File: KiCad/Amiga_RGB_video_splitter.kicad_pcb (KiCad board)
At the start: 4 copper layers, 57.5 x 60 mm, 35 parts, among them J1 DB23_Female-Connector, J2 DB15_Female_HighDensity_Mount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, J3 KMDGX-9S-BS-1, J4 PJ-320A, J5 MSS22D18 3Pin Slide Toggle Sw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, J6 MSS22D18 3Pin Slide Toggle Sw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, J7 Conn_01x01, U1 THS7374IPWR, U2 74HCT2G17, U3 74HCT2G14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

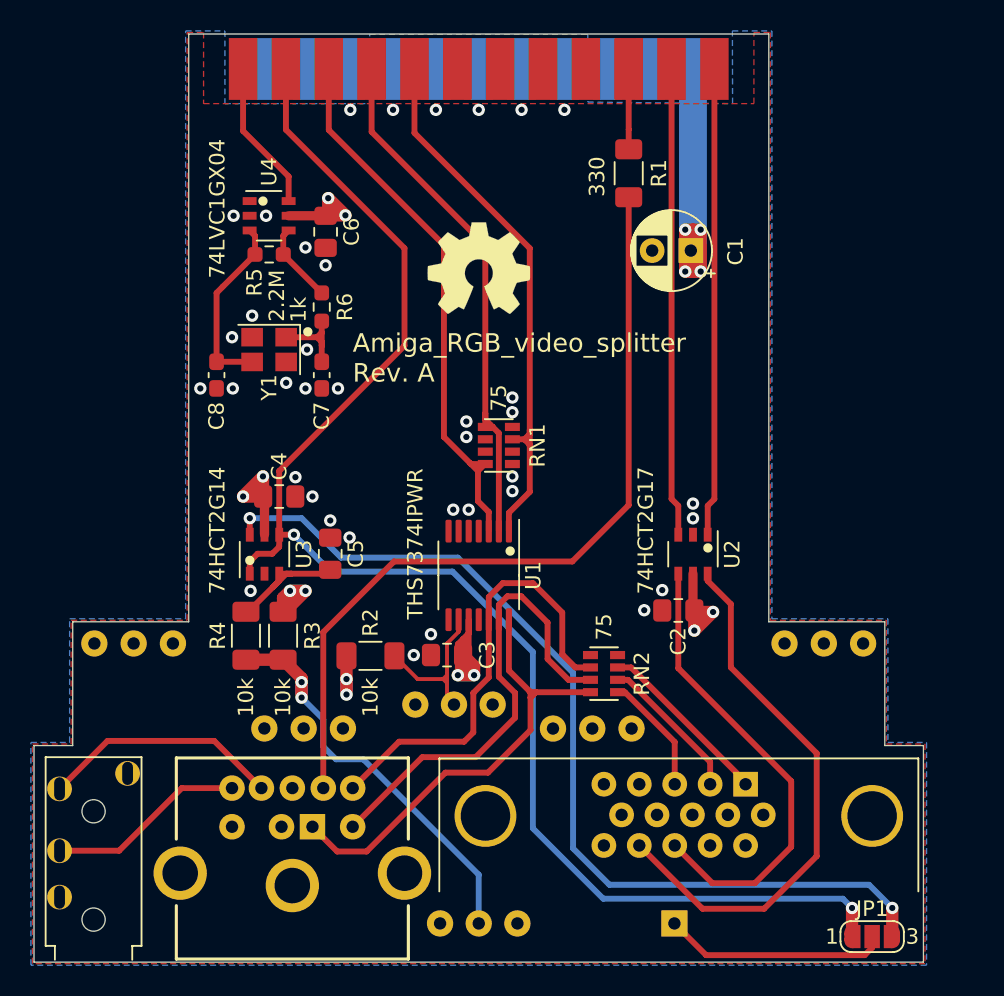
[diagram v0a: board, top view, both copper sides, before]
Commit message: Fix placement of support pinheaders and RN2, some rerouting and silkscreen fixes, bump revision to Rev B
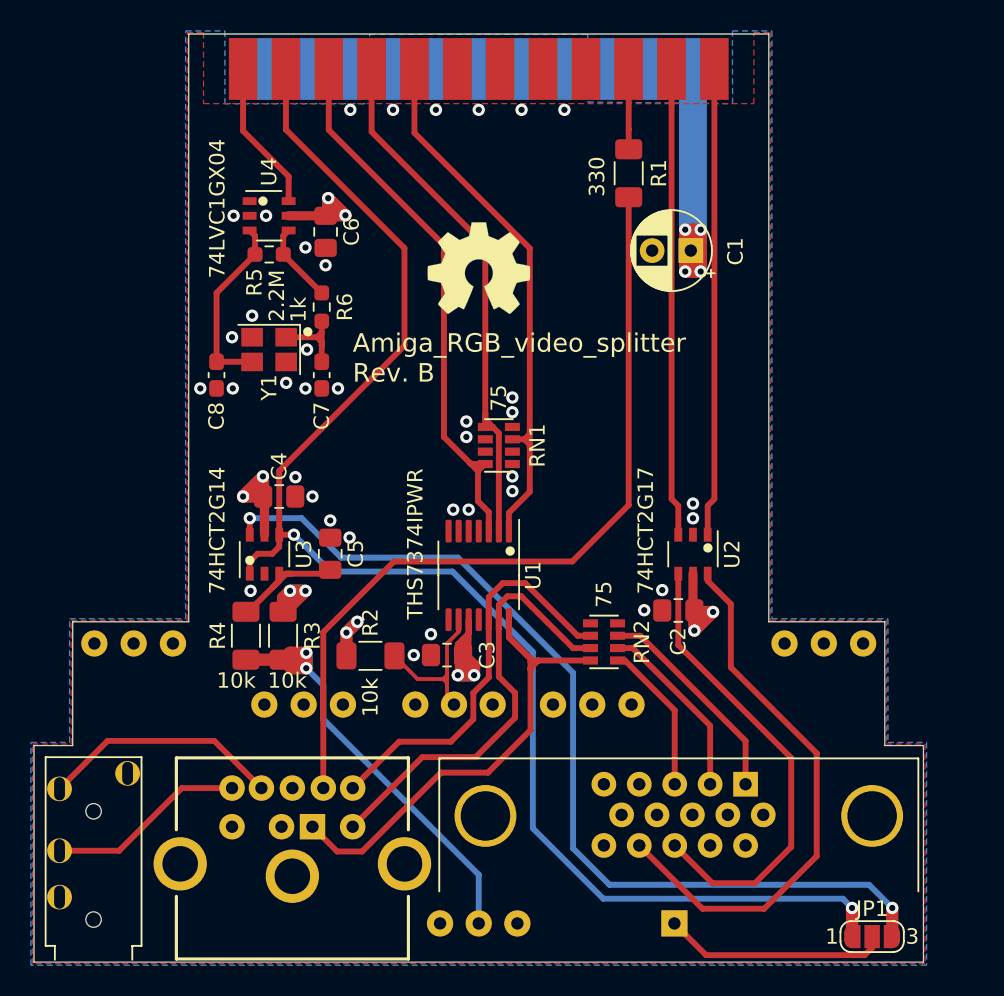
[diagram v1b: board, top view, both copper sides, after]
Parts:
- moved RN2 2.05 mm to (155.8, 124.3)
- moved REF** 1.55 mm to (152.5, 128.3)
- moved REF** 1.54 mm to (133.8, 128.3)
- moved J3 0.60 mm to (137.0, 135.6)
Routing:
- net Net-(J6-Pad2): track 26.7 -> 32.3 mm
- net RED: track 29.2 -> 26.3 mm
- net VGA_R: track 11.5 -> 13.9 mm
- net GREEN: track 30.9 -> 28.7 mm
- net VGA_G: track 9.62 -> 11.9 mm
- net BLUE: track 30.5 -> 32.6 mm
- net VGA_B: track 7.76 -> 9.81 mm
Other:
- board text added: "Amiga_RGB_video_splitter Rev. B"
- board text removed: "Amiga_RGB_video_splitter Rev. A"

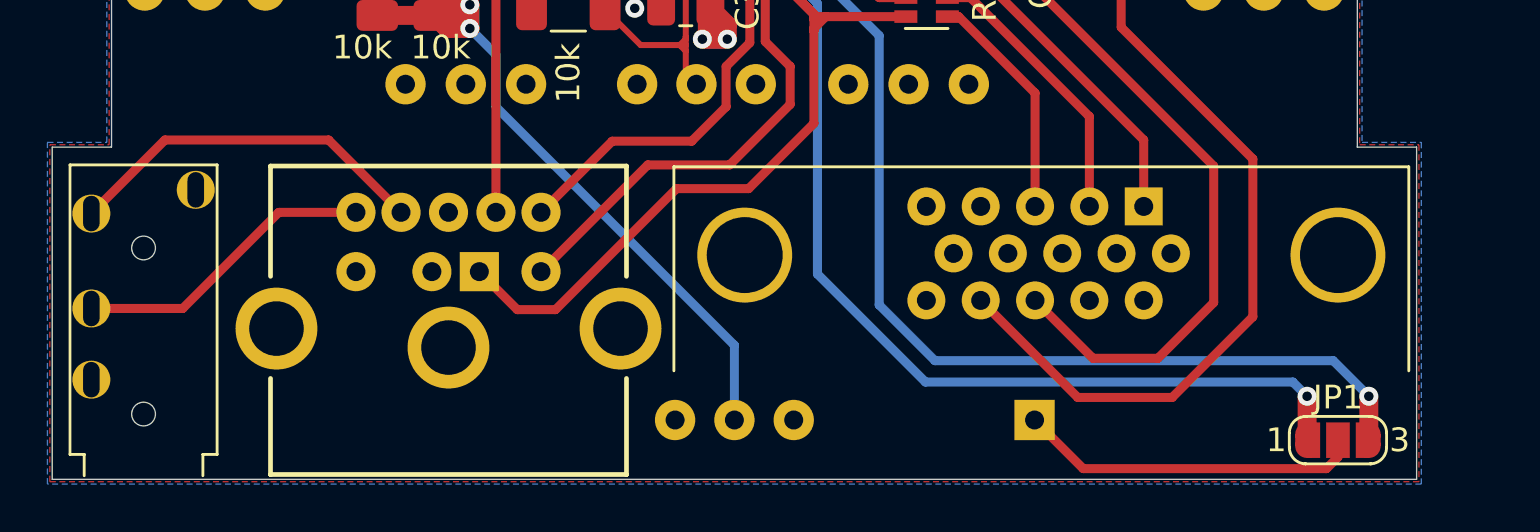
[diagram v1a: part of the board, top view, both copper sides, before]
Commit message: Relocate the PAL/NTSC 3Pin Slide Toggle Switch
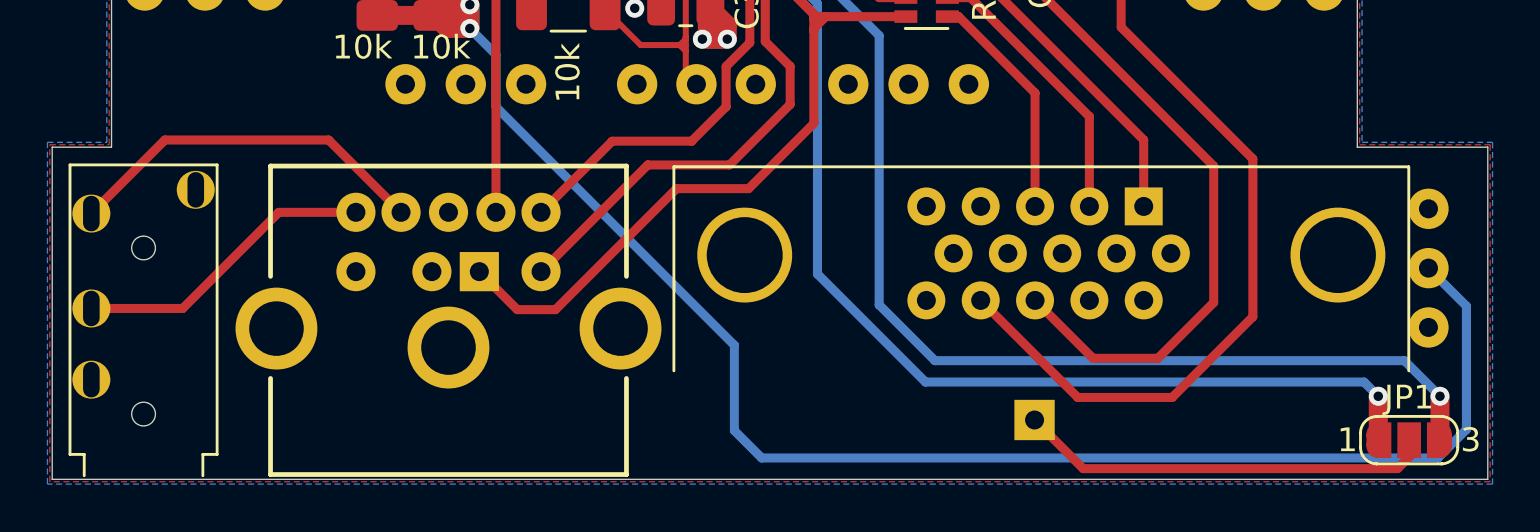
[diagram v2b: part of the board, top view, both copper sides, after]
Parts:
- moved J6 29.9 mm to (176.9, 136.1), turned to 180 degrees
- moved JP1 3.00 mm to (176.1, 143.3)
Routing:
- net Net-(J6-Pad2): track 32.3 -> 72.1 mm
- net OE: track 61.5 -> 64.5 mm
- net XCLKEN: track 96.1 -> 99.1 mm
- net Net-(J7-Pad1): track 14.6 -> 17.6 mm
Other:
- board size 57.5 x 60 mm -> 60.5 x 60 mm

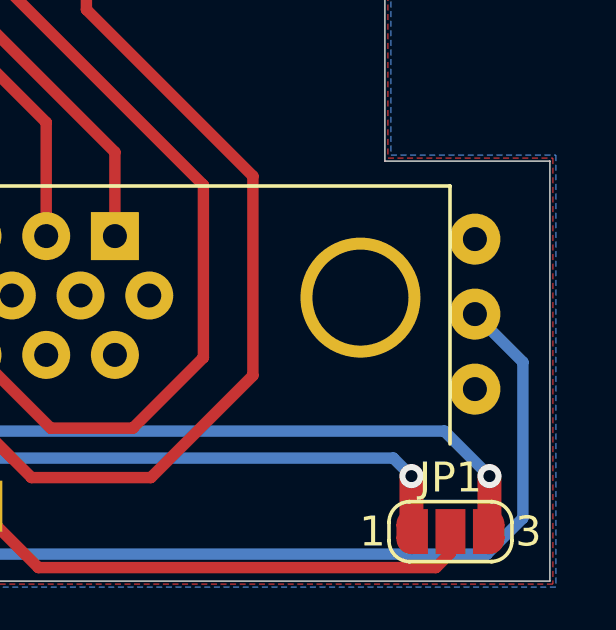
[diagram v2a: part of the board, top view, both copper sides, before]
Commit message: Silkscreen fix on VGA connector footprint
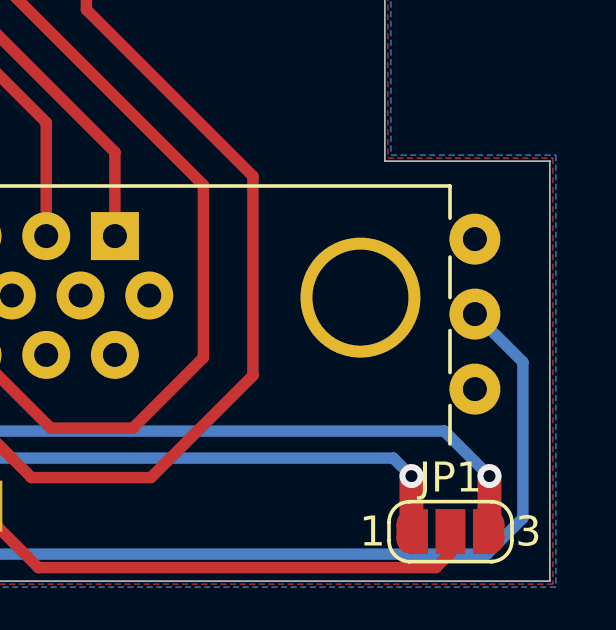
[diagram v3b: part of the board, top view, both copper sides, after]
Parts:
- J6: moved to F.Cu

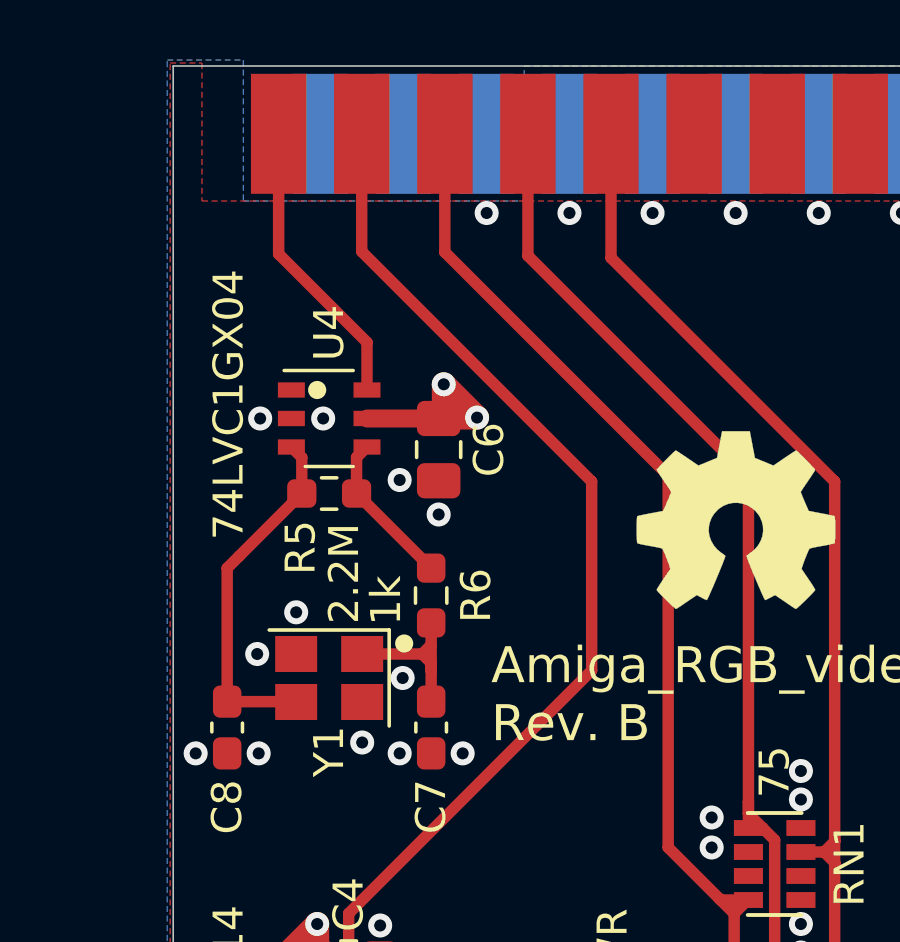
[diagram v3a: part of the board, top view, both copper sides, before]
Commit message: Add damping 150 Ohm series resistor on XCLK out, bump to Rev. C
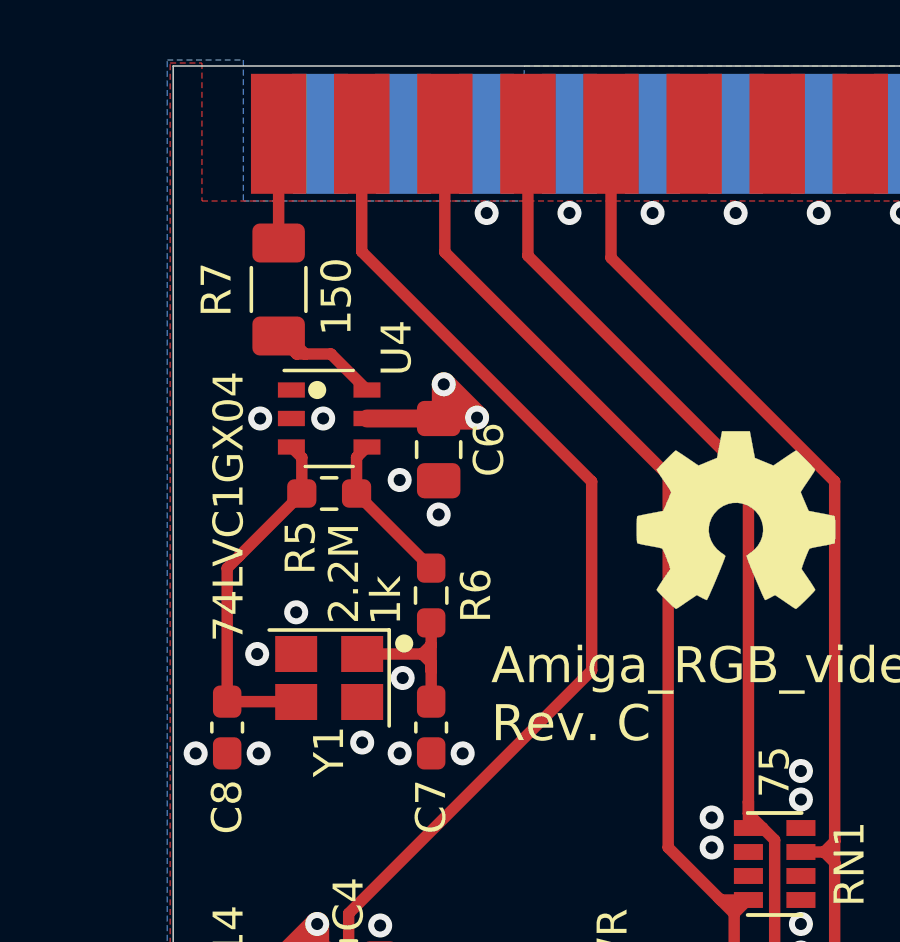
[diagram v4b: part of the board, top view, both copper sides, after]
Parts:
- added R7: 150, Resistor_SMD:R_1206_3216Metric_Pad1.30x1.75mm_HandSolder, F.Cu at (132.5, 92.5)
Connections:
- U4 pad 6: XCLK -> Net-(R7-Pad1)
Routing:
- net XCLK: track 9.76 -> 3.64 mm
- net Net-(R7-Pad1): track 0.00 -> 4.82 mm
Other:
- board text added: "150"
- board text added: "Amiga_RGB_video_splitter Rev. C"
- board text removed: "Amiga_RGB_video_splitter Rev. B"
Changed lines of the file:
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@@
   (general
     (thickness 1.6)
-    (drawings 31)
-    (tracks 345)
+    (drawings 32)
+    (tracks 349)
     (zones 0)
-    (modules 35)
-    (nets 57)
+    (modules 36)
+    (nets 58)
   )
   (page A4)
@@
   (net 55 "Net-(C8-Pad1)")
   (net 56 "Net-(J7-Pad1)")
+  (net 57 "Net-(R7-Pad1)")
   (net_class Default "This is the default net class."
     (clearance 0.1524)
@@
     (add_net "Net-(J7-Pad1)")
     (add_net "Net-(R5-Pad2)")
+    (add_net "Net-(R7-Pad1)")
     (add_net "Net-(RN1-Pad3)")
     (add_net "Net-(RN1-Pad6)")
@@
     (add_net XCLK)
     (add_net XCLKEN)
+  )
+  (module Resistor_SMD:R_1206_3216Metric_Pad1.30x1.75mm_HandSolder (layer F.Cu)
+    (at 132.465 92.45 90)
+    (descr "Resistor SMD 1206 (3216 Metric), square (rectangular) end terminal, IPC_7351 nominal with elongated pad for handsoldering. (Body size source: IPC-SM-782 page 72, https://www.pcb-3d.com/wordpress/wp-content/uploads/ipc-sm-782a_amendment_1_and_2.pdf), generated with kicad-footprint-generator")
+    (tags "resistor handsolder")
+    (attr smd)
+    (fp_text reference R7 (at 0 -2.065 90) (layer F.SilkS)
+      (effects (font (size 1 1) (thickness 0.15)))
+    )
+    (fp_text value 150 (at 0 1.82 90) (layer F.Fab) hide
+      (effects (font (size 1 1) (thickness 0.15)))
+    )
+    (fp_line (start 2.45 1.12) (end -2.45 1.12) (layer F.CrtYd) (width 0.05))
+    (fp_line (start 2.45 -1.12) (end 2.45 1.12) (layer F.CrtYd) (width 0.05))
+    (fp_line (start -2.45 -1.12) (end 2.45 -1.12) (layer F.CrtYd) (width 0.05))
+    (fp_line (start -2.45 1.12) (end -2.45 -1.12) (layer F.CrtYd) (width 0.05))
+    (fp_line (start -0.727064 0.91) (end 0.727064 0.91) (layer F.SilkS) (width 0.12))
+    (fp_line (start -0.727064 -0.91) (end 0.727064 -0.91) (layer F.SilkS) (width 0.12))
+    (fp_line (start 1.6 0.8) (end -1.6 0.8) (layer F.Fab) (width 0.1))
+    (fp_line (start 1.6 -0.8) (end 1.6 0.8) (layer F.Fab) (width 0.1))
+    (fp_line (start -1.6 -0.8) (end 1.6 -0.8) (layer F.Fab) (width 0.1))
+    (fp_line (start -1.6 0.8) (end -1.6 -0.8) (layer F.Fab) (width 0.1))
+    (fp_text user %R (at 0 0 90) (layer F.Fab) hide
+      (effects (font (size 0.8 0.8) (thickness 0.12)))
+    )
+    (pad 2 smd roundrect (at 1.55 0 90) (size 1.3 1.75) (layers F.Cu F.Paste F.Mask) (roundrect_rratio 0.192308)
+      (net 18 XCLK))
+    (pad 1 smd roundrect (at -1.55 0 90) (size 1.3 1.75) (layers F.Cu F.Paste F.Mask) (roundrect_rratio 0.192308)
+      (net 57 "Net-(R7-Pad1)"))
+    (model ${KISYS3DMOD}/Resistor_SMD.3dshapes/R_1206_3216Metric.wrl
+      (at (xyz 0 0 0))
+      (scale (xyz 1 1 1))
+      (rotate (xyz 0 0 0))
+    )
   )
   (module Connector_Dsub:DSUB-15-HD_Female_Horizontal_P2.29x1.98mm_EdgePinOffset3.03mm_Housed_MountingHolesOffset4.94mm (layer F.Cu)
@@
     (tags "Jedec MO-193C TSOP-6L")
     (attr smd)
-    (fp_text reference U4 (at 0 -2.85 90) (layer F.SilkS)
+    (fp_text reference U4 (at 2.25 -2.35 90) (layer F.SilkS)
       (effects (font (size 1 1) (thickness 0.15)))
     )
@@
     )
     (pad 6 smd rect (at 1.26 -0.95) (size 0.9 0.51) (layers F.Cu F.Paste F.Mask)
-      (net 18 XCLK))
+      (net 57 "Net-(R7-Pad1)"))
     (pad 5 smd rect (at 1.26 0) (size 0.9 0.51) (layers F.Cu F.Paste F.Mask)
       (net 2 VCC))
@@
       (xy 0.555814 -2.531069)) (layer F.SilkS) (width 0.01))
   )
+  (gr_text 150 (at 134.4 94 90) (layer F.SilkS)
+    (effects (font (size 1 1) (thickness 0.15)) (justify left))
+  )
   (dimension 8 (width 0.15) (layer Dwgs.User)
     (gr_text "8.000 mm" (at 177.85 127 270) (layer Dwgs.User)
@@
     (arrow2b (pts (xy 118.95 155.7) (xy 120.076504 155.113579)))
   )
-  (gr_text "Amiga_RGB_video_splitter\nRev. B" (at 139.55 105.95) (layer F.SilkS)
+  (gr_text "Amiga_RGB_video_splitter\nRev. C" (at 139.55 105.95) (layer F.SilkS)
     (effects (font (size 1.2 1.2) (thickness 0.2)) (justify left))
   )
@@
     (effects (font (size 1 1) (thickness 0.15)) (justify left))
   )
-  (gr_text 74LVC1GX04 (at 130.8 100.8 90) (layer F.SilkS)
+  (gr_text 74LVC1GX04 (at 130.8 104.2 90) (layer F.SilkS)
     (effects (font (size 1 1) (thickness 0.15)) (justify left))
   )
@@
   (segment (start 139.15 123.7) (end 139.85 123) (width 0.8) (layer F.Cu) (net 2))
   (segment (start 139.15 123.7) (end 139.85 123) (width 0.8) (layer B.Cu) (net 2))
-  (segment (start 132.465 87.26) (end 132.465 91.265) (width 0.381) (layer F.Cu) (net 18))
-  (segment (start 135.41 94.21) (end 135.41 95.8) (width 0.381) (layer F.Cu) (net 18))
-  (segment (start 132.465 91.265) (end 135.41 94.21) (width 0.381) (layer F.Cu) (net 18))
+  (segment (start 132.465 87.26) (end 132.465 90.9) (width 0.381) (layer F.Cu) (net 18))
   (segment (start 135.235 87.26) (end 135.235 91.185) (width 0.381) (layer F.Cu) (net 19))
   (segment (start 135.235 91.185) (end 142.9 98.85) (width 0.381) (layer F.Cu) (net 19))
@@
   (segment (start 175.65 144.55) (end 176.135 144.065) (width 0.381) (layer F.Cu) (net 56))
   (segment (start 162.4 144.55) (end 175.65 144.55) (width 0.381) (layer F.Cu) (net 56))
+  (segment (start 134.21 94.6) (end 135.41 95.8) (width 0.381) (layer F.Cu) (net 57))
+  (segment (start 132.465 94) (end 133.065 94.6) (width 0.381) (layer F.Cu) (net 57))
+  (segment (start 132.75 94) (end 133.35 94.6) (width 0.381) (layer F.Cu) (net 57))
+  (segment (start 132.465 94) (end 132.75 94) (width 0.381) (layer F.Cu) (net 57))
+  (segment (start 133.35 94.6) (end 134.21 94.6) (width 0.381) (layer F.Cu) (net 57))
+  (segment (start 133.065 94.6) (end 133.35 94.6) (width 0.381) (layer F.Cu) (net 57))
   (zone (net 1) (net_name GND) (layer F.Cu) (hatch edge 0.508)
     (connect_pads (clearance 0.1524))
